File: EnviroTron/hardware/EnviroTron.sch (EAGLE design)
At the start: 29 parts

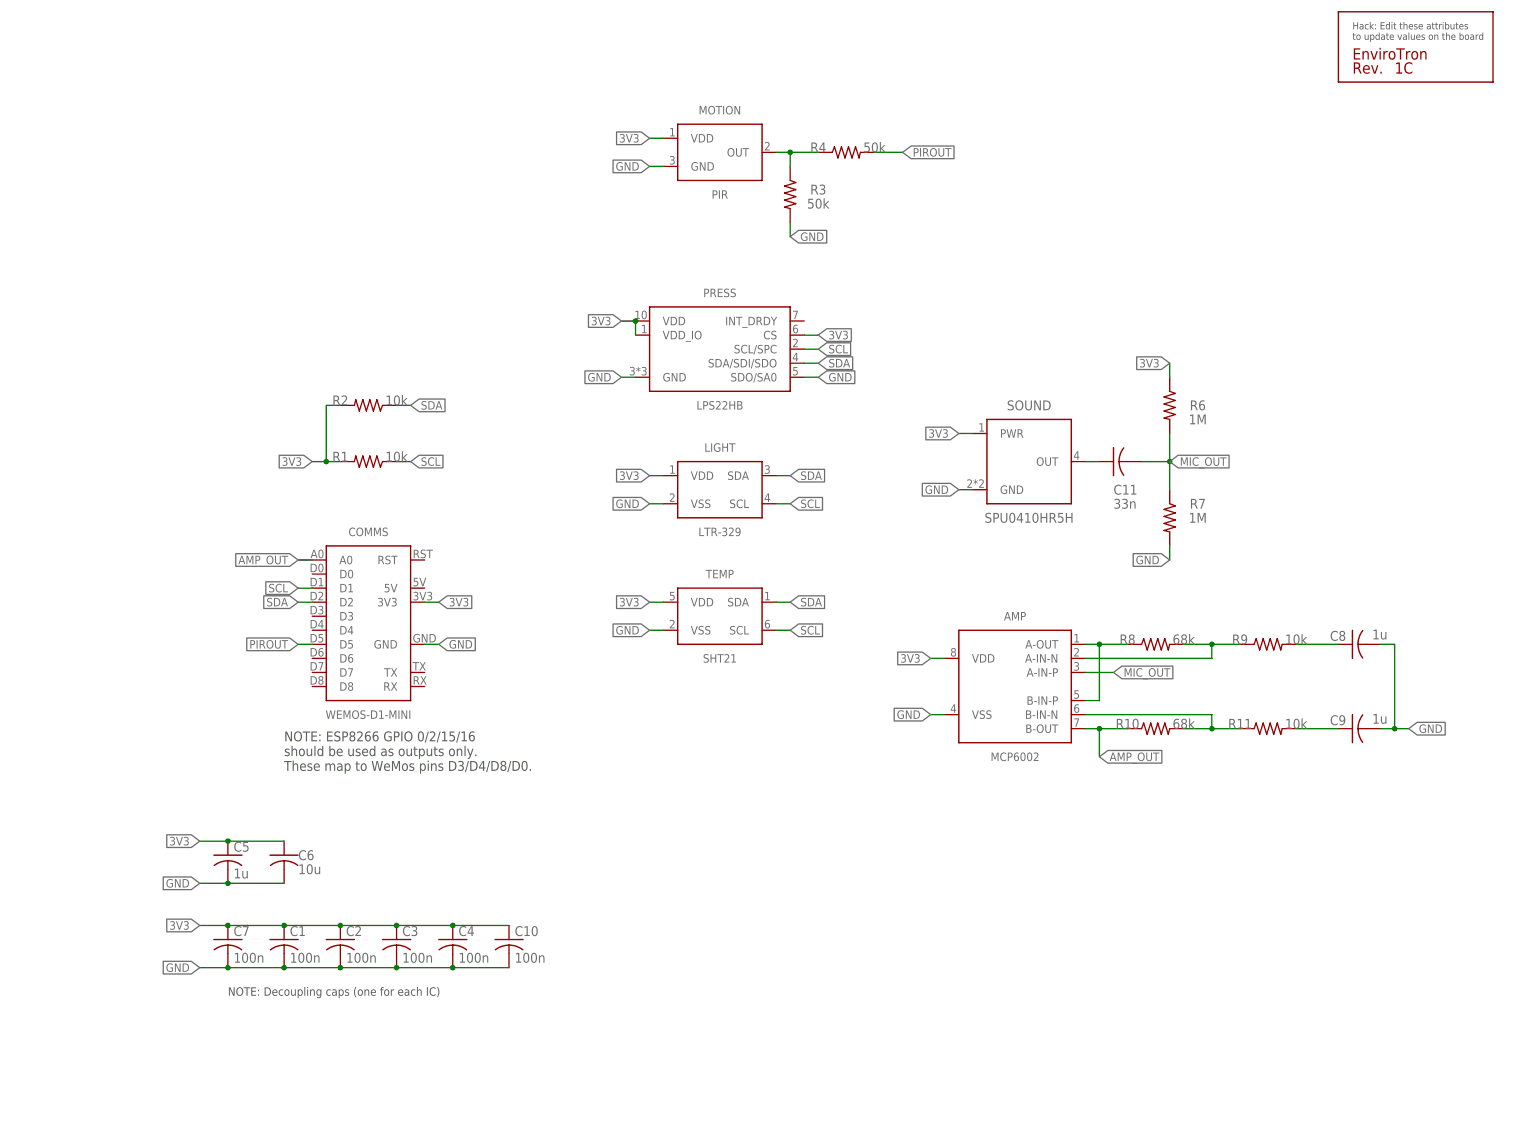
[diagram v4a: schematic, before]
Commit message: Added 3v3 regulator; finalized layout and BOM
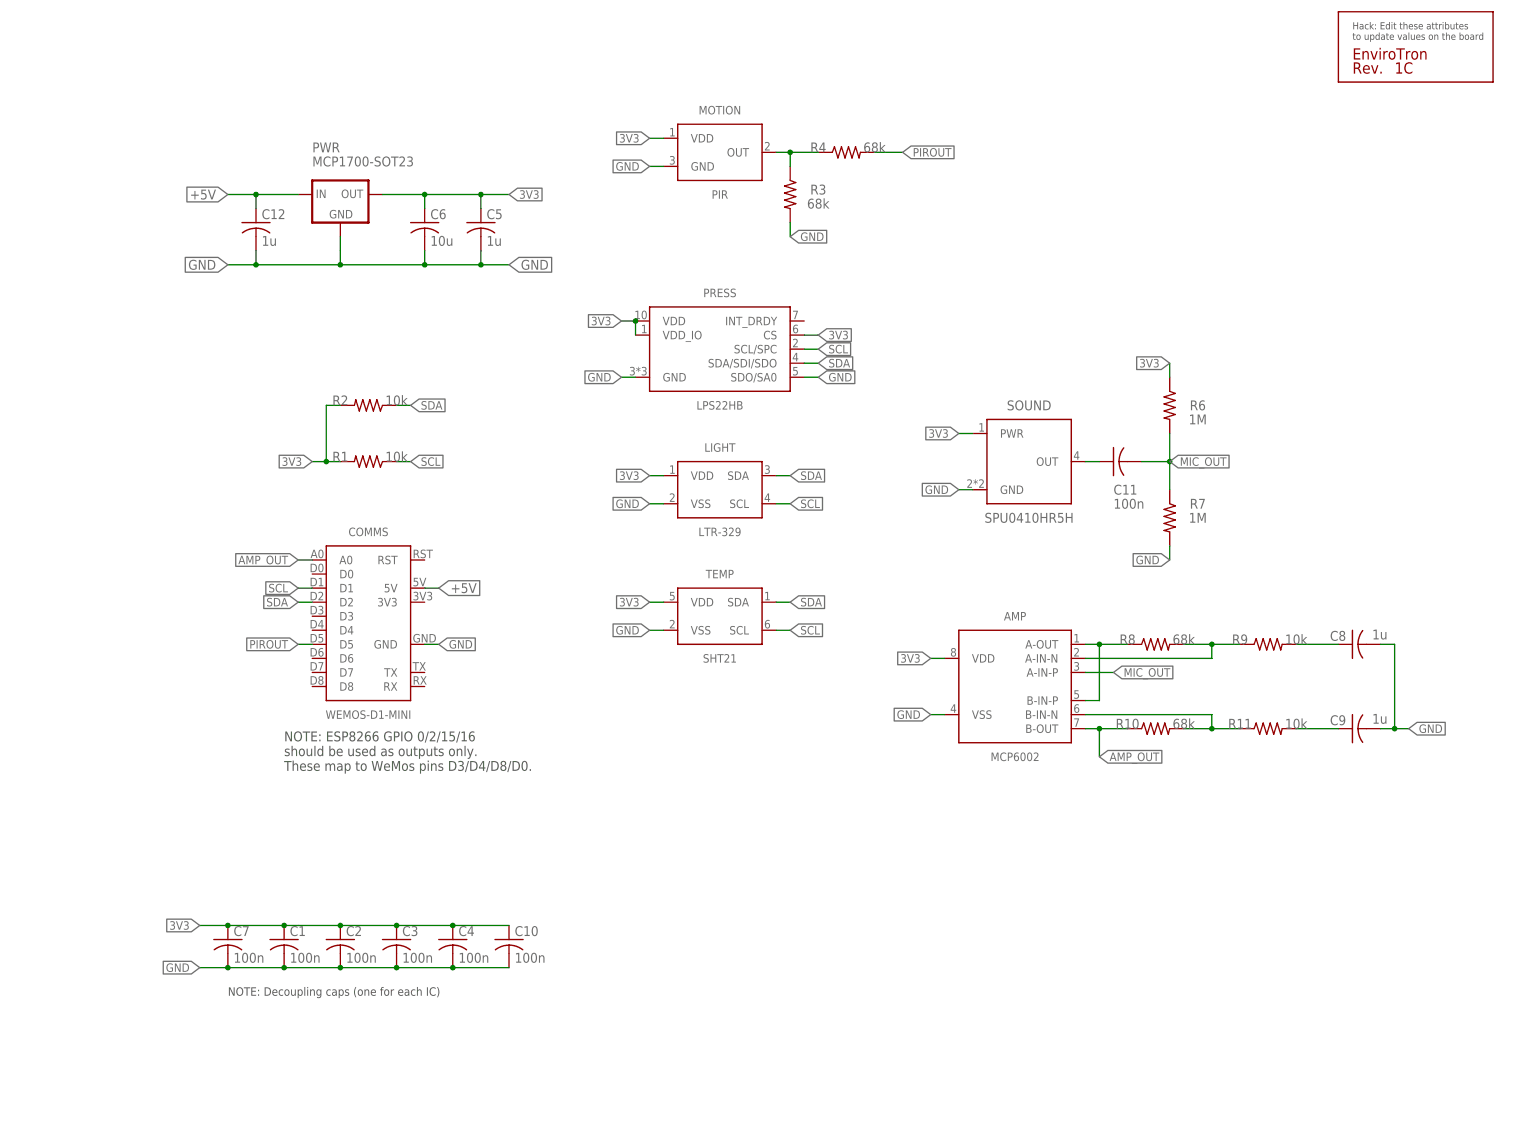
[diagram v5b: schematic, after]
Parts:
- added C12: 1u, EnviroTron:C-USC0603
- added PWR: MCP1700-SOT23, EnviroTron:MCP1700-SOT23
- C11: value 33n -> 100n
- C6: device rcl:C-USC0805 -> EnviroTron:C-USC0805
- R3, R4: value 50k -> 68k
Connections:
- new net +5V: C12.1, COMMS.5V, PWR.IN
- net 3V3: now also PWR.OUT; no longer COMMS.3V3
- net GND: now also C12.2, PWR.GND
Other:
- moved on the sheet: C5
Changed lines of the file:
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@@
 <part name="R2" library="EnviroTron" deviceset="R-US_" device="R0603" value="10k"/>
 <part name="C5" library="EnviroTron" deviceset="C-US" device="C0603" value="1u"/>
-<part name="C6" library="rcl" deviceset="C-US" device="C0805" value="10u"/>
+<part name="C6" library="EnviroTron" deviceset="C-US" device="C0805" value="10u"/>
 <part name="MOTION" library="EnviroTron" deviceset="PIR" device=""/>
-<part name="R3" library="EnviroTron" deviceset="R-US_" device="R0603" value="50k"/>
+<part name="R3" library="EnviroTron" deviceset="R-US_" device="R0603" value="68k"/>
 <part name="TEMP" library="EnviroTron" deviceset="SHT21" device=""/>
 <part name="COMMS" library="EnviroTron" deviceset="WEMOS-D1-MINI" device=""/>
@@
 <part name="R10" library="EnviroTron" deviceset="R-US_" device="R0603" value="68k"/>
 <part name="R11" library="EnviroTron" deviceset="R-US_" device="R0603" value="10k"/>
-<part name="C11" library="EnviroTron" deviceset="C-US" device="C0603" value="33n"/>
+<part name="C11" library="EnviroTron" deviceset="C-US" device="C0603" value="100n"/>
 <part name="FRAME1" library="EnviroTron" deviceset="LETTER_L" device="">
 <attribute name="SECTION" value="Sensor Board"/>
@@
 </part>
 <part name="C10" library="EnviroTron" deviceset="C-US" device="C0603" value="100n"/>
-<part name="R4" library="EnviroTron" deviceset="R-US_" device="R0603" value="50k"/>
+<part name="R4" library="EnviroTron" deviceset="R-US_" device="R0603" value="68k"/>
+<part name="PWR" library="EnviroTron" deviceset="MCP1700" device="-SOT23"/>
+<part name="C12" library="EnviroTron" deviceset="C-US" device="C0603" value="1u"/>
 </parts>
 <sheets>
@@
 <attribute name="VALUE" x="50.8" y="114.3" size="1.778" layer="96" align="bottom-center"/>
 </instance>
-<instance part="C5" gate="G$1" x="20.32" y="33.02"/>
-<instance part="C6" gate="G$1" x="30.48" y="33.02"/>
+<instance part="C5" gate="G$1" x="66.04" y="147.32"/>
+<instance part="C6" gate="G$1" x="55.88" y="147.32"/>
 <instance part="MOTION" gate="G$1" x="109.22" y="160.02"/>
 <instance part="R3" gate="G$1" x="121.92" y="152.4" smashed="yes" rot="R270">
@@
 <attribute name="VALUE" x="137.16" y="160.02" size="1.778" layer="96" align="bottom-center"/>
 </instance>
+<instance part="PWR" gate="G$1" x="40.64" y="149.86" smashed="yes">
+<attribute name="NAME" x="35.56" y="160.02" size="1.778" layer="95"/>
+<attribute name="VALUE" x="35.56" y="157.48" size="1.778" layer="96"/>
+</instance>
+<instance part="C12" gate="G$1" x="25.4" y="147.32"/>
 </instances>
 <busses>
@@
 <net name="3V3" class="0">
 <segment>
-<wire x1="55.88" y1="78.74" x2="58.42" y2="78.74" width="0.1524" layer="91"/>
-<label x="58.42" y="78.74" size="1.524" layer="95" xref="yes"/>
-<pinref part="COMMS" gate="G$1" pin="3V3"/>
+<label x="71.12" y="152.4" size="1.524" layer="95" xref="yes"/>
+<wire x1="71.12" y1="152.4" x2="66.04" y2="152.4" width="0.1524" layer="91"/>
+<pinref part="C6" gate="G$1" pin="1"/>
+<wire x1="66.04" y1="152.4" x2="55.88" y2="152.4" width="0.1524" layer="91"/>
+<wire x1="55.88" y1="152.4" x2="48.26" y2="152.4" width="0.1524" layer="91"/>
+<wire x1="55.88" y1="149.86" x2="55.88" y2="152.4" width="0.1524" layer="91"/>
+<junction x="55.88" y="152.4"/>
+<pinref part="C5" gate="G$1" pin="1"/>
+<wire x1="66.04" y1="149.86" x2="66.04" y2="152.4" width="0.1524" layer="91"/>
+<junction x="66.04" y="152.4"/>
+<pinref part="PWR" gate="G$1" pin="OUT"/>
 </segment>
 <segment>
@@
 </segment>
 <segment>
-<wire x1="20.32" y1="35.56" x2="15.24" y2="35.56" width="0.1524" layer="91"/>
-<label x="15.24" y="35.56" size="1.524" layer="95" rot="R180" xref="yes"/>
-<pinref part="C6" gate="G$1" pin="1"/>
-<pinref part="C5" gate="G$1" pin="1"/>
-<wire x1="20.32" y1="35.56" x2="30.48" y2="35.56" width="0.1524" layer="91"/>
-<junction x="20.32" y="35.56"/>
-</segment>
-<segment>
 <pinref part="R6" gate="G$1" pin="1"/>
 <wire x1="190.5" y1="121.92" x2="190.5" y2="119.38" width="0.1524" layer="91"/>
@@
 </segment>
 <segment>
-<wire x1="20.32" y1="27.94" x2="15.24" y2="27.94" width="0.1524" layer="91"/>
-<label x="15.24" y="27.94" size="1.524" layer="95" rot="R180" xref="yes"/>
-<pinref part="C6" gate="G$1" pin="2"/>
-<pinref part="C5" gate="G$1" pin="2"/>
-<wire x1="20.32" y1="27.94" x2="30.48" y2="27.94" width="0.1524" layer="91"/>
-<junction x="20.32" y="27.94"/>
-</segment>
-<segment>
 <pinref part="R7" gate="G$1" pin="2"/>
 <wire x1="190.5" y1="88.9" x2="190.5" y2="86.36" width="0.1524" layer="91"/>
@@
 <label x="233.68" y="55.88" size="1.524" layer="95" xref="yes"/>
 </segment>
+<segment>
+<wire x1="40.64" y1="144.78" x2="40.64" y2="142.24" width="0.1524" layer="91"/>
+<pinref part="C6" gate="G$1" pin="2"/>
+<wire x1="55.88" y1="142.24" x2="55.88" y2="139.7" width="0.1524" layer="91"/>
+<wire x1="55.88" y1="139.7" x2="40.64" y2="139.7" width="0.1524" layer="91"/>
+<wire x1="40.64" y1="139.7" x2="40.64" y2="142.24" width="0.1524" layer="91"/>
+<pinref part="C5" gate="G$1" pin="2"/>
+<wire x1="66.04" y1="142.24" x2="66.04" y2="139.7" width="0.1524" layer="91"/>
+<wire x1="66.04" y1="139.7" x2="55.88" y2="139.7" width="0.1524" layer="91"/>
+<junction x="55.88" y="139.7"/>
+<wire x1="66.04" y1="139.7" x2="71.12" y2="139.7" width="0.1524" layer="91"/>
+<junction x="66.04" y="139.7"/>
+<label x="71.12" y="139.7" size="1.778" layer="95" xref="yes"/>
+<pinref part="PWR" gate="G$1" pin="GND"/>
+<pinref part="C12" gate="G$1" pin="2"/>
+<wire x1="40.64" y1="139.7" x2="25.4" y2="139.7" width="0.1524" layer="91"/>
+<wire x1="25.4" y1="139.7" x2="25.4" y2="142.24" width="0.1524" layer="91"/>
+<junction x="40.64" y="139.7"/>
+<wire x1="25.4" y1="139.7" x2="20.32" y2="139.7" width="0.1524" layer="91"/>
+<junction x="25.4" y="139.7"/>
+<label x="20.32" y="139.7" size="1.778" layer="95" rot="R180" xref="yes"/>
+</segment>
 </net>
 <net name="PIROUT" class="0">
@@
 </segment>
 </net>
+<net name="+5V" class="0">
+<segment>
+<wire x1="33.02" y1="152.4" x2="25.4" y2="152.4" width="0.1524" layer="91"/>
+<label x="20.32" y="152.4" size="1.778" layer="95" rot="R180" xref="yes"/>
+<pinref part="PWR" gate="G$1" pin="IN"/>
+<pinref part="C12" gate="G$1" pin="1"/>
+<wire x1="25.4" y1="152.4" x2="20.32" y2="152.4" width="0.1524" layer="91"/>
+<wire x1="25.4" y1="149.86" x2="25.4" y2="152.4" width="0.1524" layer="91"/>
+<junction x="25.4" y="152.4"/>
+</segment>
+<segment>
+<pinref part="COMMS" gate="G$1" pin="5V"/>
+<wire x1="55.88" y1="81.28" x2="58.42" y2="81.28" width="0.1524" layer="91"/>
+<label x="58.42" y="81.28" size="1.778" layer="95" xref="yes"/>
+</segment>
+</net>

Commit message: Added ADC in place of noisy ESP8266 ADC. Switched to precision reference for voltage source.
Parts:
- added C13: 100n, EnviroTron:C-USC0603
- added C14, C15: 1n, EnviroTron:C-USC0603
- added U2: MCP3221, EnviroTron:MCP3221
- PWR: value MCP1700-SOT23 -> VREG-REF33XX-SOT23; device EnviroTron:MCP1700-SOT23 -> EnviroTron:VREG-REF33XX-SOT23
- U$1: REV 1C -> 1D
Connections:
- net 3V3: now also C13.1, U2.VDD
- net AMP_OUT: now also C15.1, U2.AIN; no longer COMMS.A0
- net GND: now also C13.2, U2.VSS
- net N$2: now also C14.1
- net N$6: now also C14.2
- net N$9: now also C15.2
- net SCL: now also U2.SCL
- net SDA: now also U2.SDA
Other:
- moved on the sheet: R6, R7
